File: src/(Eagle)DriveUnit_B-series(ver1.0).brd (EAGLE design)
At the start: 65.7 x 51 mm, 55 parts, among them IC1 A3921, SW1 TVAF06-A020B-R, SW2 TVAF06-A020B-R, SW3 THAF01-NC-R, SW4 SS-12D00G3

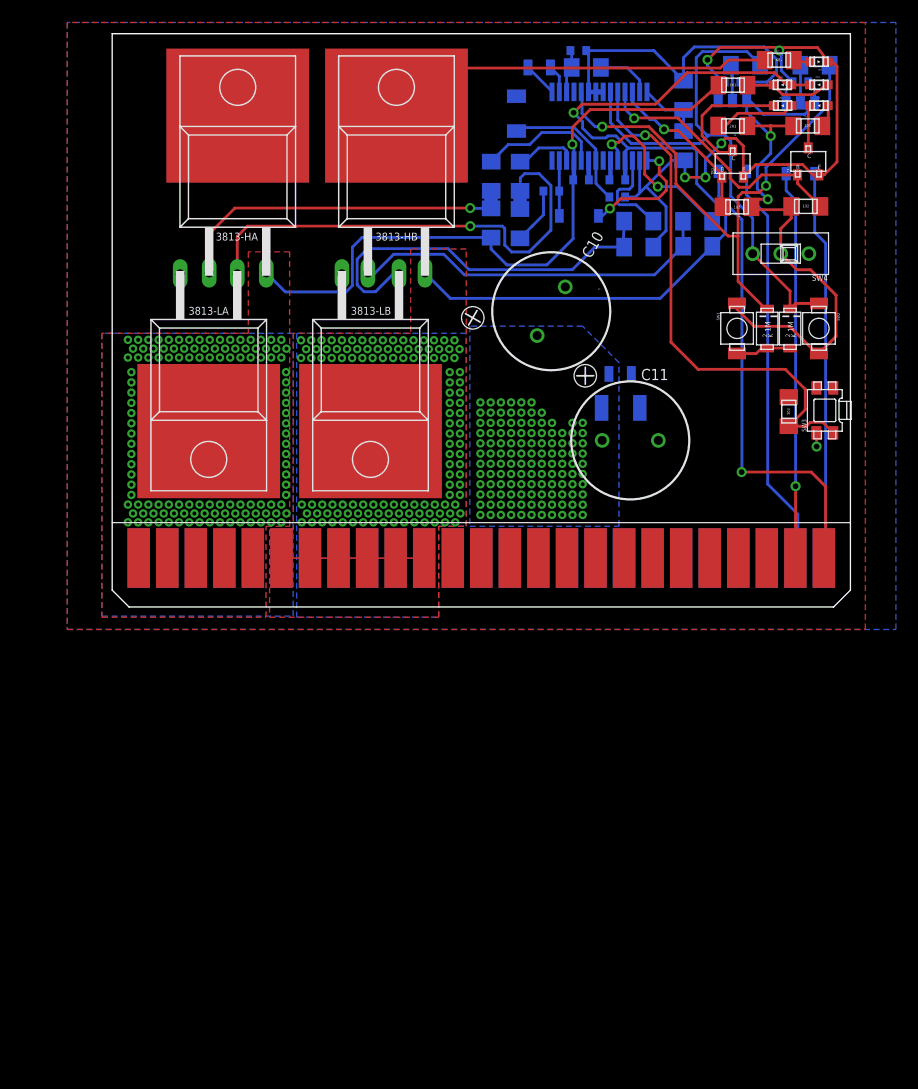
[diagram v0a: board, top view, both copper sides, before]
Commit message: [fix]入力周りなどの変更(ver1.0の問題点の修復)
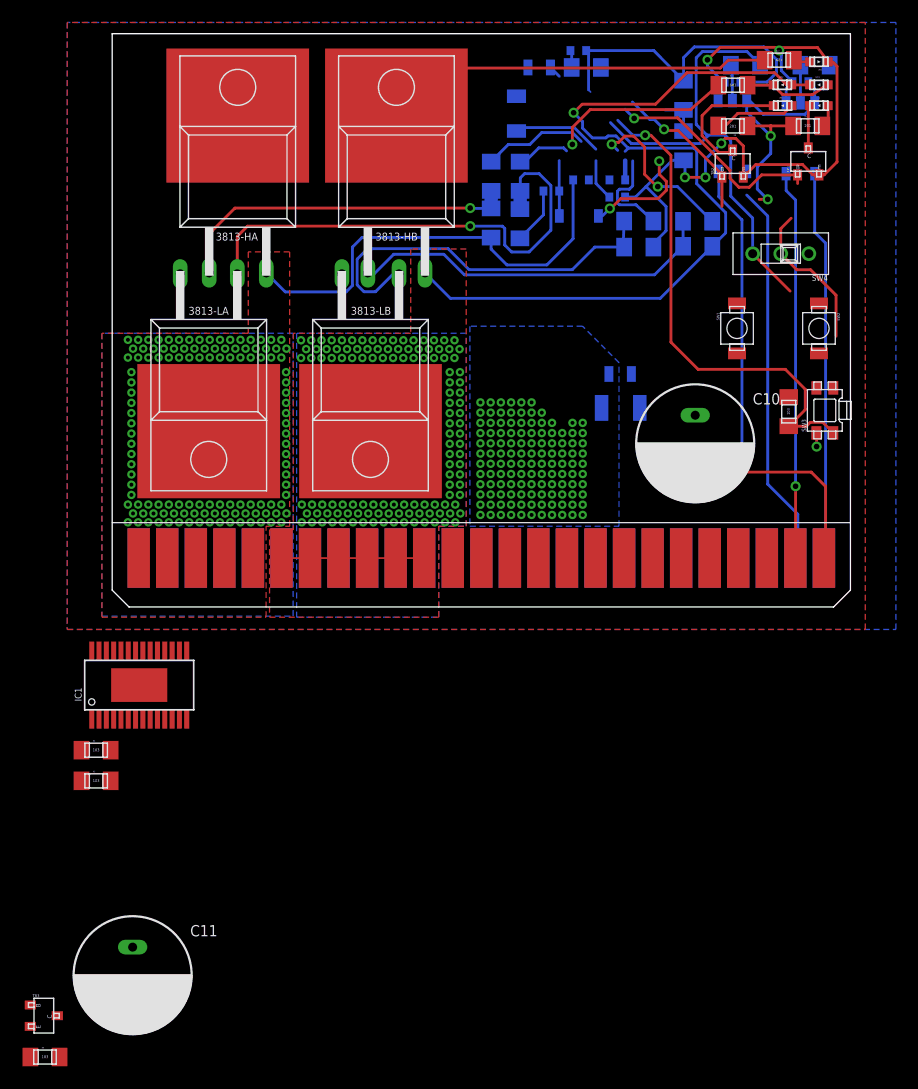
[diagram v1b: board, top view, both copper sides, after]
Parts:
- removed D8, D9: GS1010FL, GS1010FL:GS1010FL
- added R4: RG2012, RG2012:RG2012
- added TR3: 2SC3325, 2SC3325:2SC3325
- R5, R6: value RG2012-N-102-B-T5 -> RG2012; device RG2012-N-102-B-T5:RG2012 -> RG2012:RG2012
- moved R6 99.2 mm to (-7.28, -40.0), turned to 0 degrees
- moved R5 81.2 mm to (-2.73, -15.5)
- moved IC1 70.1 mm to (-1.82, -9.10), flipped to the top
- moved C11 65.0 mm to (1.82, -32.8), turned to 0 degrees
- moved C10 17.4 mm to (51.9, 14.6), turned to 0 degrees
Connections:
- removed net N$12: D8.A, D9.A, SW1.RIGHT
- net DIR: now also R9.LEFT, SW1.RIGHT, TR3.B; no longer D8.C
- net FF1: now also R4.LEFT; no longer R5.RIGHT
- net FF2: now also R5.LEFT; no longer R6.RIGHT
- net GND: now also IC1.PAD, SW1.LEFT, TR3.E
- net GND_IN: now also TLP2.3
- net PWM: now also R6.RIGHT, TR3.C; no longer D9.C, R9.LEFT, SW2.LEFT
- net PWM_IN: now also TLP2.1; no longer TLP2.3
- net V5: now also R4.RIGHT, R5.RIGHT; no longer R5.LEFT, SW1.LEFT, SW2.RIGHT
- net VCC_IN: no longer TLP2.1
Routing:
- net DIR: track 49.0 -> 0.00 mm, vias 2 -> 0
- net V5: track 89.8 -> 70.5 mm
- net PWM: track 48.5 -> 41.4 mm
- net N$16: track 4.97 -> 0.00 mm
- net N$12: track 4.93 -> 0.00 mm
- net GND: track 79.5 -> 74.9 mm
- net FF1: track 24.3 -> 19.9 mm
- net N$1: track 3.07 -> 0.00 mm
- net SA: track 59.0 -> 56.1 mm
- net RESET: track 47.2 -> 44.7 mm
- net N$4: track 5.79 -> 3.53 mm
- net VCC_IN: track 36.4 -> 34.3 mm
- net N$3: track 1.76 -> 0.00 mm
- net N$15: track 1.73 -> 0.00 mm
- net GHA: track 11.1 -> 9.41 mm
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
